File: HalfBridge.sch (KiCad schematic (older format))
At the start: 9 parts, among them Q20 DMN62D0U-7, Q21 DMN62D0U-7, Q4 STS8DN6LF6AG

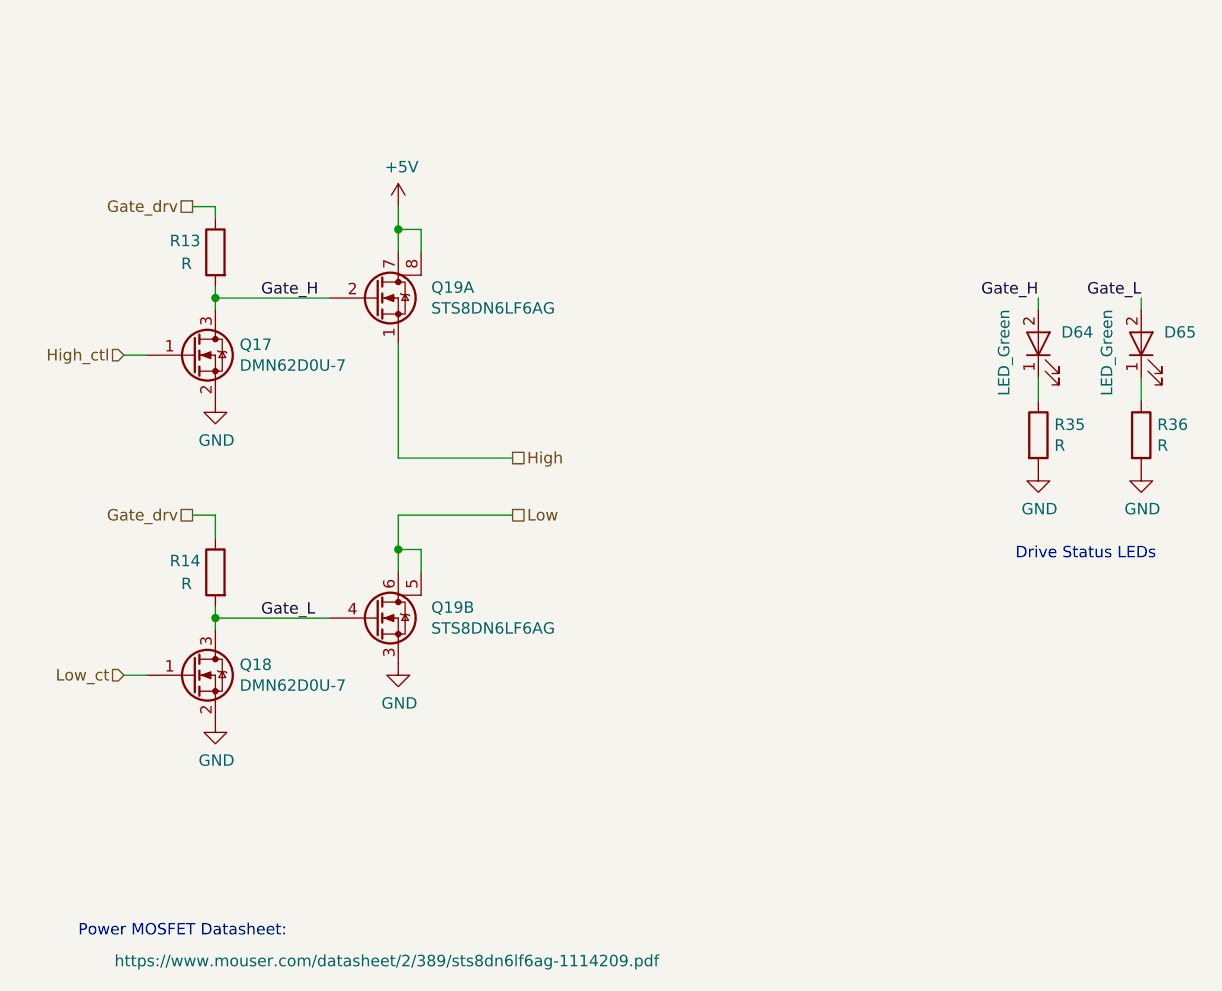
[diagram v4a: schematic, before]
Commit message: Added Current Sensor to Schematic
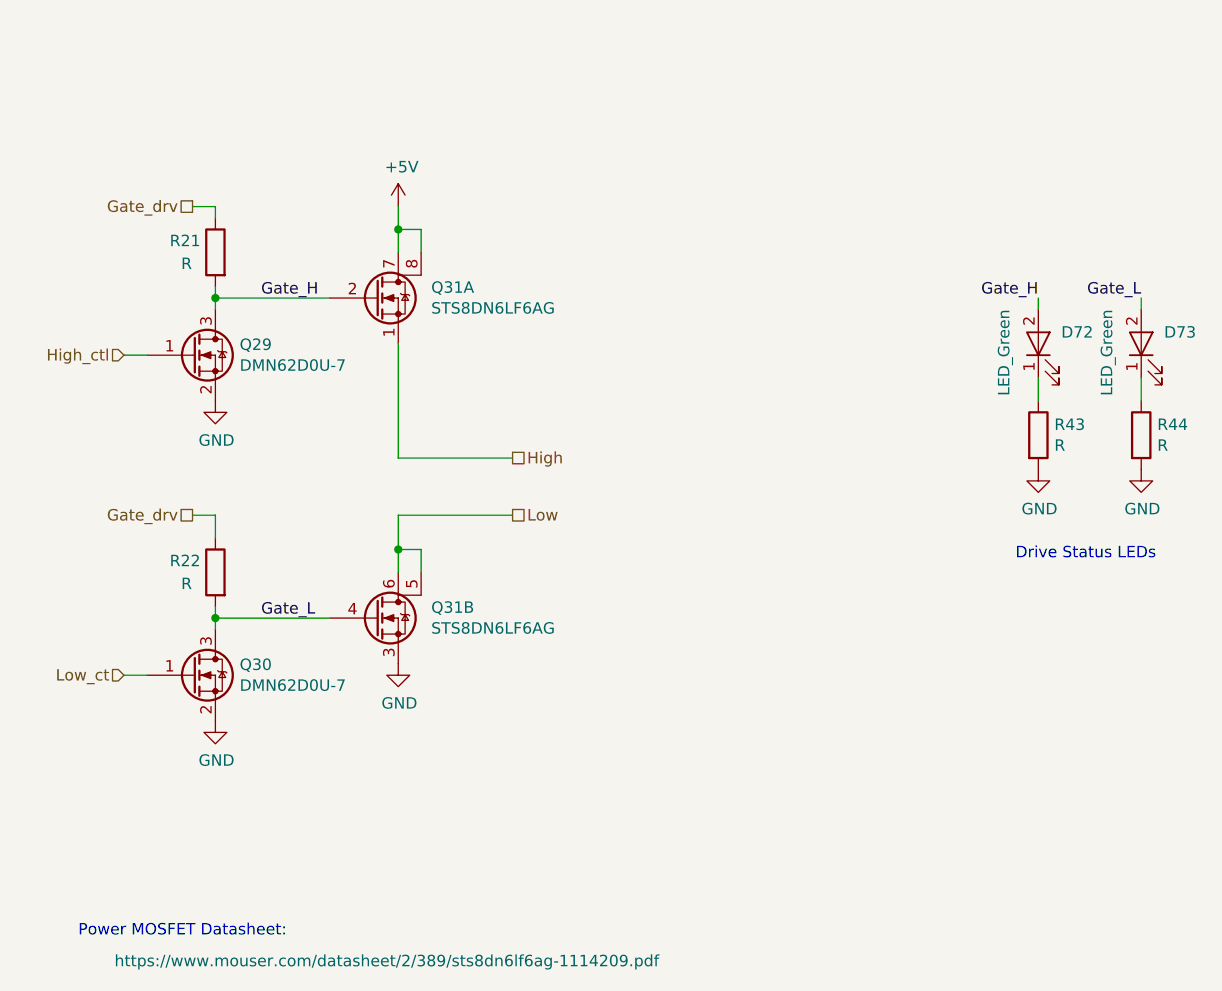
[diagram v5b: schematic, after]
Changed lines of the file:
@@
 AR Path="/5EEA5FAB/5EE98773" Ref="R19"  Part="1"
 AR Path="/5EEA5FB2/5EE98773" Ref="R21"  Part="1"
-F 0 "R13" H 4000 2850 50  0000 R CNN
+F 0 "R21" H 4000 2850 50  0000 R CNN
 F 1 "R" H 3950 2750 50  0000 R CNN
 F 2 "Resistor_SMD:R_0805_2012Metric" V 3730 2800 50  0001 C CNN
@@
 AR Path="/5EEA5FAB/5EE9878C" Ref="R20"  Part="1"
 AR Path="/5EEA5FB2/5EE9878C" Ref="R22"  Part="1"
-F 0 "R14" H 4000 4250 50  0000 R CNN
+F 0 "R22" H 4000 4250 50  0000 R CNN
 F 1 "R" H 3950 4150 50  0000 R CNN
 F 2 "Resistor_SMD:R_0805_2012Metric" V 3730 4200 50  0001 C CNN
@@
 AR Path="/5EEA5FAB/5EE9879E" Ref="Q28"  Part="1"
 AR Path="/5EEA5FB2/5EE9879E" Ref="Q31"  Part="1"
-F 0 "Q19" H 4744 3046 50  0000 L CNN
+F 0 "Q31" H 4744 3046 50  0000 L CNN
 F 1 "STS8DN6LF6AG" H 4744 2955 50  0000 L CNN
 F 2 "Custom-Footprints:SO-8_3.9x4.9mm_P1.27mm" H 4250 3500 50  0001 C CNN
@@
 AR Path="/5EEA5FAB/5EE987A9" Ref="Q28"  Part="2"
 AR Path="/5EEA5FB2/5EE987A9" Ref="Q31"  Part="2"
-F 0 "Q19" H 4744 4446 50  0000 L CNN
+F 0 "Q31" H 4744 4446 50  0000 L CNN
 F 1 "STS8DN6LF6AG" H 4744 4355 50  0000 L CNN
 F 2 "Custom-Footprints:SO-8_3.9x4.9mm_P1.27mm" H 4250 4900 50  0001 C CNN
@@
 AR Path="/5EEA5FA4/5F3B0E6C" Ref="D68"  Part="1"
 AR Path="/5EEA5FB2/5F3B0E6C" Ref="D72"  Part="1"
-F 0 "D64" V 7450 3100 50  0000 R CNN
+F 0 "D72" V 7450 3100 50  0000 R CNN
 F 1 "LED_Green" H 7550 3350 50  0000 R CNN
 F 2 "LED_SMD:LED_0805_2012Metric_Pad1.15x1.40mm_HandSolder" H 7750 3650 50  0001 C CNN
@@
 AR Path="/5EEA5FA4/5F3B0E72" Ref="R39"  Part="1"
 AR Path="/5EEA5FB2/5F3B0E72" Ref="R43"  Part="1"
-F 0 "R35" H 7470 3646 50  0000 L CNN
+F 0 "R43" H 7470 3646 50  0000 L CNN
 F 1 "R" H 7470 3555 50  0000 L CNN
 F 2 "Resistor_SMD:R_0805_2012Metric" V 7330 3600 50  0001 C CNN
@@
 AR Path="/5EEA5FA4/5F3B0E85" Ref="D69"  Part="1"
 AR Path="/5EEA5FB2/5F3B0E85" Ref="D73"  Part="1"
-F 0 "D65" V 7900 3100 50  0000 R CNN
+F 0 "D73" V 7900 3100 50  0000 R CNN
 F 1 "LED_Green" H 8000 3350 50  0000 R CNN
 F 2 "LED_SMD:LED_0805_2012Metric_Pad1.15x1.40mm_HandSolder" H 8200 3650 50  0001 C CNN
@@
 AR Path="/5EEA5FA4/5F3B0E8B" Ref="R40"  Part="1"
 AR Path="/5EEA5FB2/5F3B0E8B" Ref="R44"  Part="1"
-F 0 "R36" H 7920 3646 50  0000 L CNN
+F 0 "R44" H 7920 3646 50  0000 L CNN
 F 1 "R" H 7920 3555 50  0000 L CNN
 F 2 "Resistor_SMD:R_0805_2012Metric" V 7780 3600 50  0001 C CNN
@@
 AR Path="/5EEA5FAB/5F506CAB" Ref="Q26"  Part="1"
 AR Path="/5EEA5FB2/5F506CAB" Ref="Q29"  Part="1"
-F 0 "Q17" H 3906 3296 50  0000 L CNN
+F 0 "Q29" H 3906 3296 50  0000 L CNN
 F 1 "DMN62D0U-7" H 3906 3205 50  0000 L CNN
 F 2 "Package_TO_SOT_SMD:SOT-23" H 3450 3950 50  0001 C CNN
@@
 AR Path="/5EEA5FAB/5F506FFC" Ref="Q27"  Part="1"
 AR Path="/5EEA5FB2/5F506FFC" Ref="Q30"  Part="1"
-F 0 "Q18" H 3906 4696 50  0000 L CNN
+F 0 "Q30" H 3906 4696 50  0000 L CNN
 F 1 "DMN62D0U-7" H 3906 4605 50  0000 L CNN
 F 2 "Package_TO_SOT_SMD:SOT-23" H 3450 5350 50  0001 C CNN

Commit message: Updated Pins to match routes
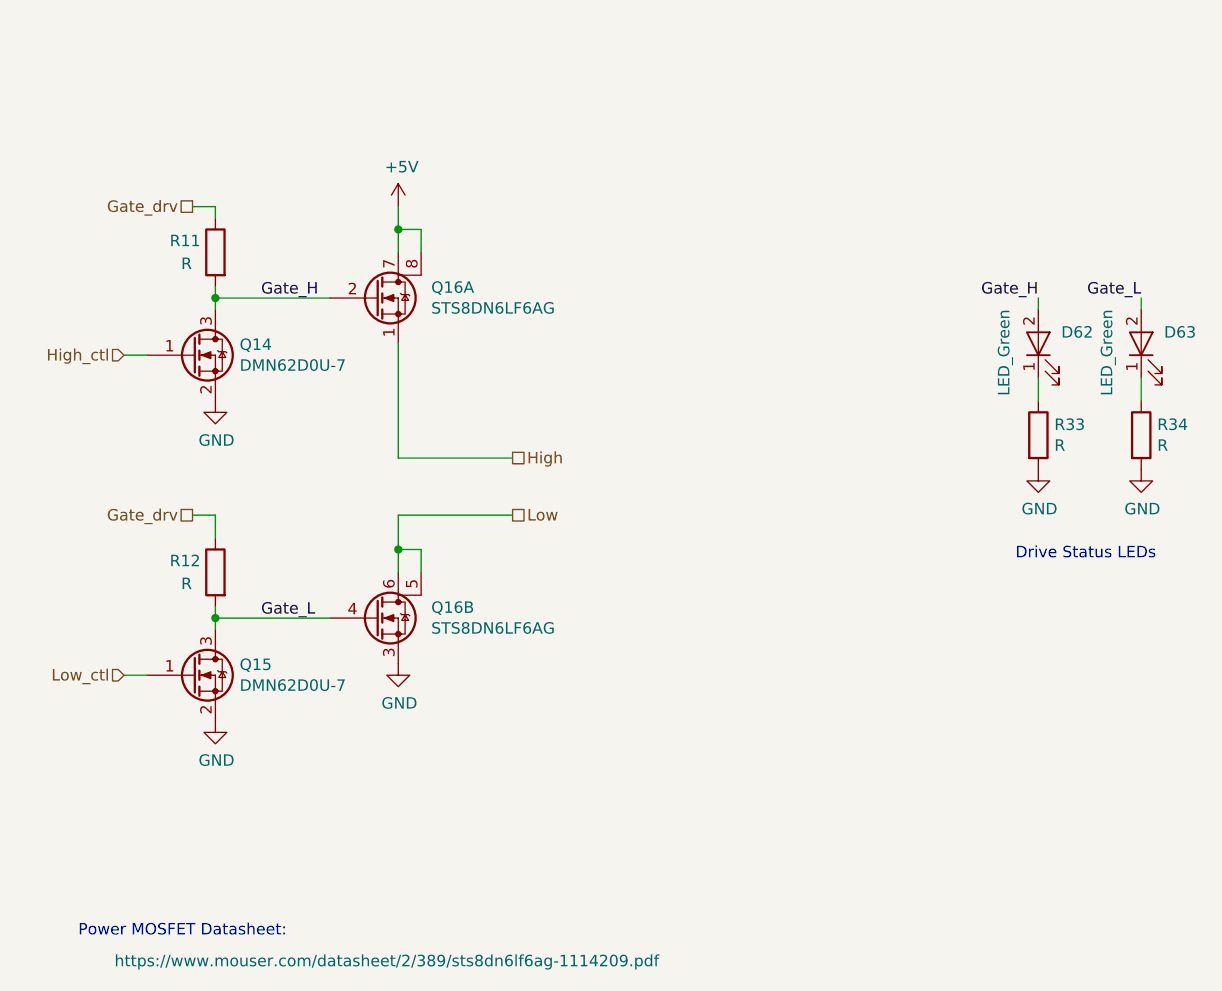
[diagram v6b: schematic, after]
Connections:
- net Low_ct renamed Low_ctl
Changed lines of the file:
@@
 $Descr A 11000 8500
 encoding utf-8
-Sheet 8 12
+Sheet 7 12
 Title "Flip Pixel Board"
 Date "2020-06-20"
@@
 AR Path="/5EEA5FAB/5EE98773" Ref="R19"  Part="1"
 AR Path="/5EEA5FB2/5EE98773" Ref="R21"  Part="1"
-F 0 "R21" H 4000 2850 50  0000 R CNN
+F 0 "R11" H 4000 2850 50  0000 R CNN
 F 1 "R" H 3950 2750 50  0000 R CNN
 F 2 "Resistor_SMD:R_0805_2012Metric" V 3730 2800 50  0001 C CNN
@@
 AR Path="/5EEA5FAB/5EE9878C" Ref="R20"  Part="1"
 AR Path="/5EEA5FB2/5EE9878C" Ref="R22"  Part="1"
-F 0 "R22" H 4000 4250 50  0000 R CNN
+F 0 "R12" H 4000 4250 50  0000 R CNN
 F 1 "R" H 3950 4150 50  0000 R CNN
 F 2 "Resistor_SMD:R_0805_2012Metric" V 3730 4200 50  0001 C CNN
@@
 AR Path="/5EEA5FAB/5EE9879E" Ref="Q28"  Part="1"
 AR Path="/5EEA5FB2/5EE9879E" Ref="Q31"  Part="1"
-F 0 "Q31" H 4744 3046 50  0000 L CNN
+F 0 "Q16" H 4744 3046 50  0000 L CNN
 F 1 "STS8DN6LF6AG" H 4744 2955 50  0000 L CNN
 F 2 "Custom-Footprints:SO-8_3.9x4.9mm_P1.27mm" H 4250 3500 50  0001 C CNN
@@
 AR Path="/5EEA5FAB/5EE987A9" Ref="Q28"  Part="2"
 AR Path="/5EEA5FB2/5EE987A9" Ref="Q31"  Part="2"
-F 0 "Q31" H 4744 4446 50  0000 L CNN
+F 0 "Q16" H 4744 4446 50  0000 L CNN
 F 1 "STS8DN6LF6AG" H 4744 4355 50  0000 L CNN
 F 2 "Custom-Footprints:SO-8_3.9x4.9mm_P1.27mm" H 4250 4900 50  0001 C CNN
@@
 High_ctl
 Text HLabel 3400 4650 0    50   Input ~ 0
-Low_ct
+Low_ctl
 Text HLabel 5100 3950 2    50   UnSpc ~ 0
 Low
@@
 AR Path="/5EEA5FA4/5F3B0E6C" Ref="D68"  Part="1"
 AR Path="/5EEA5FB2/5F3B0E6C" Ref="D72"  Part="1"
-F 0 "D72" V 7450 3100 50  0000 R CNN
+F 0 "D62" V 7450 3100 50  0000 R CNN
 F 1 "LED_Green" H 7550 3350 50  0000 R CNN
 F 2 "LED_SMD:LED_0805_2012Metric_Pad1.15x1.40mm_HandSolder" H 7750 3650 50  0001 C CNN
@@
 AR Path="/5EEA5FA4/5F3B0E72" Ref="R39"  Part="1"
 AR Path="/5EEA5FB2/5F3B0E72" Ref="R43"  Part="1"
-F 0 "R43" H 7470 3646 50  0000 L CNN
+F 0 "R33" H 7470 3646 50  0000 L CNN
 F 1 "R" H 7470 3555 50  0000 L CNN
 F 2 "Resistor_SMD:R_0805_2012Metric" V 7330 3600 50  0001 C CNN
@@
 AR Path="/5EEA5FA4/5F3B0E85" Ref="D69"  Part="1"
 AR Path="/5EEA5FB2/5F3B0E85" Ref="D73"  Part="1"
-F 0 "D73" V 7900 3100 50  0000 R CNN
+F 0 "D63" V 7900 3100 50  0000 R CNN
 F 1 "LED_Green" H 8000 3350 50  0000 R CNN
 F 2 "LED_SMD:LED_0805_2012Metric_Pad1.15x1.40mm_HandSolder" H 8200 3650 50  0001 C CNN
@@
 AR Path="/5EEA5FA4/5F3B0E8B" Ref="R40"  Part="1"
 AR Path="/5EEA5FB2/5F3B0E8B" Ref="R44"  Part="1"
-F 0 "R44" H 7920 3646 50  0000 L CNN
+F 0 "R34" H 7920 3646 50  0000 L CNN
 F 1 "R" H 7920 3555 50  0000 L CNN
 F 2 "Resistor_SMD:R_0805_2012Metric" V 7780 3600 50  0001 C CNN
@@
 AR Path="/5EEA5FAB/5F506CAB" Ref="Q26"  Part="1"
 AR Path="/5EEA5FB2/5F506CAB" Ref="Q29"  Part="1"
-F 0 "Q29" H 3906 3296 50  0000 L CNN
+F 0 "Q14" H 3906 3296 50  0000 L CNN
 F 1 "DMN62D0U-7" H 3906 3205 50  0000 L CNN
 F 2 "Package_TO_SOT_SMD:SOT-23" H 3450 3950 50  0001 C CNN
@@
 AR Path="/5EEA5FAB/5F506FFC" Ref="Q27"  Part="1"
 AR Path="/5EEA5FB2/5F506FFC" Ref="Q30"  Part="1"
-F 0 "Q30" H 3906 4696 50  0000 L CNN
+F 0 "Q15" H 3906 4696 50  0000 L CNN
 F 1 "DMN62D0U-7" H 3906 4605 50  0000 L CNN
 F 2 "Package_TO_SOT_SMD:SOT-23" H 3450 5350 50  0001 C CNN

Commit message: Updated All Traces
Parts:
- Q4: Digikey-Part 497-17309-1-ND -> (none); Manufacturer (none) -> STMicroelectronics; Manufacturer Part (none) -> STS8DN6LF6AG; Vendor (none) -> Digikey; Vendor Part (none) -> 497-17309-1-ND
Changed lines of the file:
@@
 $Descr A 11000 8500
 encoding utf-8
-Sheet 7 12
+Sheet 12 12
 Title "Flip Pixel Board"
 Date "2020-06-20"
@@
 AR Path="/5EEA5FAB/5EE98773" Ref="R19"  Part="1"
 AR Path="/5EEA5FB2/5EE98773" Ref="R21"  Part="1"
-F 0 "R11" H 4000 2850 50  0000 R CNN
+F 0 "R21" H 4000 2850 50  0000 R CNN
 F 1 "R" H 3950 2750 50  0000 R CNN
 F 2 "Resistor_SMD:R_0805_2012Metric" V 3730 2800 50  0001 C CNN
@@
 AR Path="/5EEA5FAB/5EE9878C" Ref="R20"  Part="1"
 AR Path="/5EEA5FB2/5EE9878C" Ref="R22"  Part="1"
-F 0 "R12" H 4000 4250 50  0000 R CNN
+F 0 "R22" H 4000 4250 50  0000 R CNN
 F 1 "R" H 3950 4150 50  0000 R CNN
 F 2 "Resistor_SMD:R_0805_2012Metric" V 3730 4200 50  0001 C CNN
@@
 AR Path="/5EEA5FAB/5EE9879E" Ref="Q28"  Part="1"
 AR Path="/5EEA5FB2/5EE9879E" Ref="Q31"  Part="1"
-F 0 "Q16" H 4744 3046 50  0000 L CNN
+F 0 "Q31" H 4744 3046 50  0000 L CNN
 F 1 "STS8DN6LF6AG" H 4744 2955 50  0000 L CNN
 F 2 "Custom-Footprints:SO-8_3.9x4.9mm_P1.27mm" H 4250 3500 50  0001 C CNN
 F 3 "https://www.mouser.com/datasheet/2/389/sts8dn6lf6ag-1114209.pdf" H 4550 100 50  0000 C CNN
-F 4 "497-17309-1-ND" H 3850 3350 50  0001 C CNN "Digikey-Part"
-F 5 "X" H 4850 3050 50  0001 C CNN "Spice_Primitive"
-F 6 "STS8DN6LF6AG_Package" H 3800 3750 50  0001 C CNN "Spice_Model"
-F 7 "Y" H 4850 3050 50  0001 C CNN "Spice_Netlist_Enabled"
-F 8 "C:\\Users\\winiarcc\\Desktop\\KiCad-Libraries\\SPICE_models\\sts8dn6lf6ag_spice\\Package.LIB" H 5350 3600 50  0001 C CNN "Spice_Lib_File"
+F 4 "X" H 4850 3050 50  0001 C CNN "Spice_Primitive"
+F 5 "STS8DN6LF6AG_Package" H 3800 3750 50  0001 C CNN "Spice_Model"
+F 6 "Y" H 4850 3050 50  0001 C CNN "Spice_Netlist_Enabled"
+F 7 "C:\\Users\\winiarcc\\Desktop\\KiCad-Libraries\\SPICE_models\\sts8dn6lf6ag_spice\\Package.LIB" H 5350 3600 50  0001 C CNN "Spice_Lib_File"
+F 8 "STMicroelectronics" H 0   0   50  0001 C CNN "Manufacturer"
+F 9 "STS8DN6LF6AG" H 0   0   50  0001 C CNN "Manufacturer Part"
+F 10 "Digikey" H 0   0   50  0001 C CNN "Vendor"
+F 11 "497-17309-1-ND" H 0   0   50  0001 C CNN "Vendor Part"
 	1    4550 3000
 	1    0    0    -1
@@
 AR Path="/5EEA5FAB/5EE987A9" Ref="Q28"  Part="2"
 AR Path="/5EEA5FB2/5EE987A9" Ref="Q31"  Part="2"
-F 0 "Q16" H 4744 4446 50  0000 L CNN
+F 0 "Q31" H 4744 4446 50  0000 L CNN
 F 1 "STS8DN6LF6AG" H 4744 4355 50  0000 L CNN
 F 2 "Custom-Footprints:SO-8_3.9x4.9mm_P1.27mm" H 4250 4900 50  0001 C CNN
 F 3 "https://www.mouser.com/datasheet/2/389/sts8dn6lf6ag-1114209.pdf" H 4700 4500 50  0001 C CNN
-F 4 "497-17309-1-ND" H 3850 4750 50  0001 C CNN "Digikey-Part"
-F 5 "X" H 4850 4450 50  0001 C CNN "Spice_Primitive"
-F 6 "STS8DN6LF6AG_Package" H 3800 5150 50  0001 C CNN "Spice_Model"
-F 7 "Y" H 4850 4450 50  0001 C CNN "Spice_Netlist_Enabled"
-F 8 "C:\\Users\\winiarcc\\Desktop\\KiCad-Libraries\\SPICE_models\\sts8dn6lf6ag_spice\\Package.LIB" H 5350 5000 50  0001 C CNN "Spice_Lib_File"
+F 4 "X" H 4850 4450 50  0001 C CNN "Spice_Primitive"
+F 5 "STS8DN6LF6AG_Package" H 3800 5150 50  0001 C CNN "Spice_Model"
+F 6 "Y" H 4850 4450 50  0001 C CNN "Spice_Netlist_Enabled"
+F 7 "C:\\Users\\winiarcc\\Desktop\\KiCad-Libraries\\SPICE_models\\sts8dn6lf6ag_spice\\Package.LIB" H 5350 5000 50  0001 C CNN "Spice_Lib_File"
+F 8 "STMicroelectronics" H 0   0   50  0001 C CNN "Manufacturer"
+F 9 "STS8DN6LF6AG" H 0   0   50  0001 C CNN "Manufacturer Part"
+F 10 "Digikey" H 0   0   50  0001 C CNN "Vendor"
+F 11 "497-17309-1-ND" H 0   0   50  0001 C CNN "Vendor Part"
 	2    4550 4400
 	1    0    0    -1
@@
 AR Path="/5EEA5FA4/5F3B0E6C" Ref="D68"  Part="1"
 AR Path="/5EEA5FB2/5F3B0E6C" Ref="D72"  Part="1"
-F 0 "D62" V 7450 3100 50  0000 R CNN
+F 0 "D72" V 7450 3100 50  0000 R CNN
 F 1 "LED_Green" H 7550 3350 50  0000 R CNN
 F 2 "LED_SMD:LED_0805_2012Metric_Pad1.15x1.40mm_HandSolder" H 7750 3650 50  0001 C CNN
@@
 AR Path="/5EEA5FA4/5F3B0E72" Ref="R39"  Part="1"
 AR Path="/5EEA5FB2/5F3B0E72" Ref="R43"  Part="1"
-F 0 "R33" H 7470 3646 50  0000 L CNN
+F 0 "R43" H 7470 3646 50  0000 L CNN
 F 1 "R" H 7470 3555 50  0000 L CNN
 F 2 "Resistor_SMD:R_0805_2012Metric" V 7330 3600 50  0001 C CNN
@@
 AR Path="/5EEA5FA4/5F3B0E85" Ref="D69"  Part="1"
 AR Path="/5EEA5FB2/5F3B0E85" Ref="D73"  Part="1"
-F 0 "D63" V 7900 3100 50  0000 R CNN
+F 0 "D73" V 7900 3100 50  0000 R CNN
 F 1 "LED_Green" H 8000 3350 50  0000 R CNN
 F 2 "LED_SMD:LED_0805_2012Metric_Pad1.15x1.40mm_HandSolder" H 8200 3650 50  0001 C CNN
@@
 AR Path="/5EEA5FA4/5F3B0E8B" Ref="R40"  Part="1"
 AR Path="/5EEA5FB2/5F3B0E8B" Ref="R44"  Part="1"
-F 0 "R34" H 7920 3646 50  0000 L CNN
+F 0 "R44" H 7920 3646 50  0000 L CNN
 F 1 "R" H 7920 3555 50  0000 L CNN
 F 2 "Resistor_SMD:R_0805_2012Metric" V 7780 3600 50  0001 C CNN
@@
 AR Path="/5EEA5FAB/5F506CAB" Ref="Q26"  Part="1"
 AR Path="/5EEA5FB2/5F506CAB" Ref="Q29"  Part="1"
-F 0 "Q14" H 3906 3296 50  0000 L CNN
+F 0 "Q29" H 3906 3296 50  0000 L CNN
 F 1 "DMN62D0U-7" H 3906 3205 50  0000 L CNN
 F 2 "Package_TO_SOT_SMD:SOT-23" H 3450 3950 50  0001 C CNN
@@
 AR Path="/5EEA5FAB/5F506FFC" Ref="Q27"  Part="1"
 AR Path="/5EEA5FB2/5F506FFC" Ref="Q30"  Part="1"
-F 0 "Q15" H 3906 4696 50  0000 L CNN
+F 0 "Q30" H 3906 4696 50  0000 L CNN
 F 1 "DMN62D0U-7" H 3906 4605 50  0000 L CNN
 F 2 "Package_TO_SOT_SMD:SOT-23" H 3450 5350 50  0001 C CNN

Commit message: changed files
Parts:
- removed D70, D71: LED_Green, LED_SMD:LED_0805_2012Metric_Pad1.15x1.40mm_HandSolder, symbol Custom-Symbols:LED_Green
- removed Q20, Q21: DMN62D0U-7, Package_TO_SOT_SMD:SOT-23, symbol Custom-Symbols:DMN62D0U-7
- removed R41, R42: R, Resistor_SMD:R_0805_2012Metric, symbol Device:R
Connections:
- net +5V renamed PowerRail
- net Gate_H renamed High_ctl_OD
- net Gate_L renamed Low_ctl_OD
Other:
- note added: "5V"
- note removed: "Drive Status LEDs"
- moved on the sheet: Q4A, Q4B, R3, R4
